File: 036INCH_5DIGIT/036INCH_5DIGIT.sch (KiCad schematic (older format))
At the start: 10 parts, among them J1 Conn_01x04_Female, J2 Conn_01x04_Male, U2 TM1637

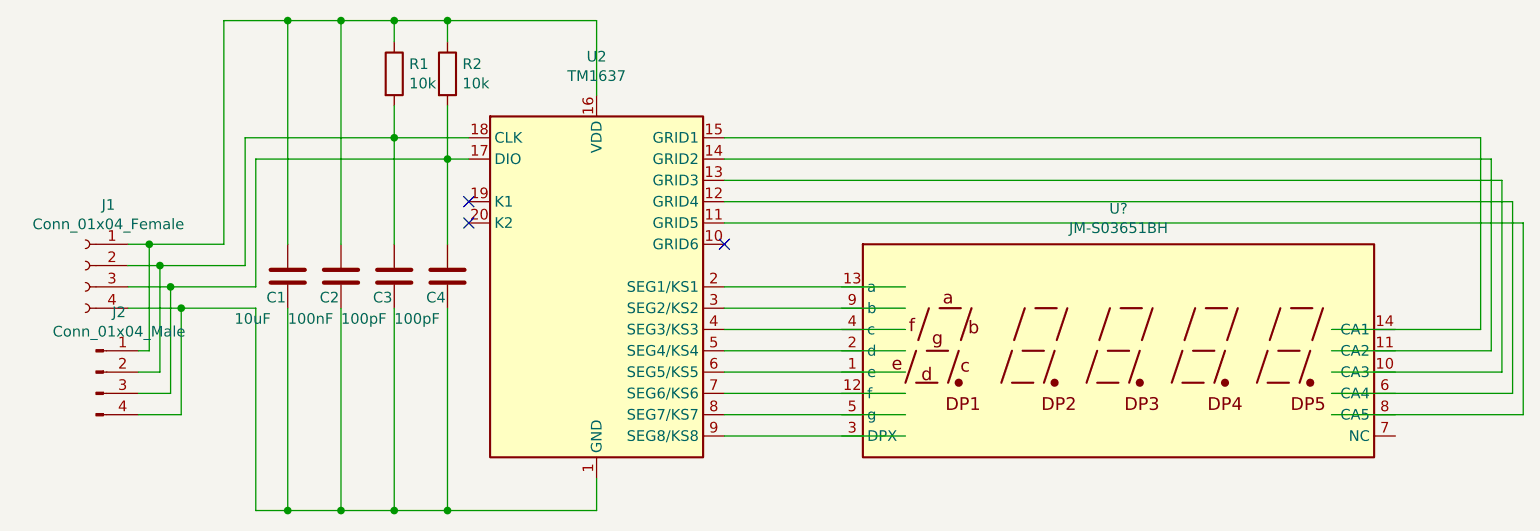
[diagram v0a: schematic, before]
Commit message: jingmei display symbol finished
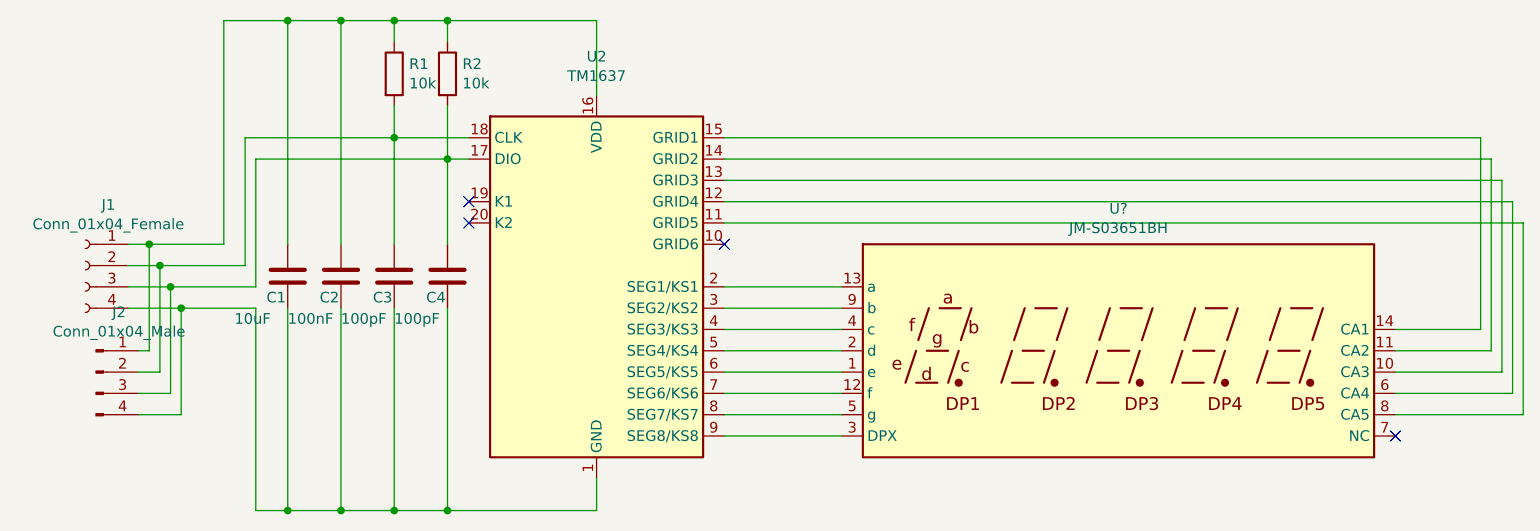
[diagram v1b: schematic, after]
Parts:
- removed U?: JM-S03651BH, JINGMEI:JM-S03651BH, symbol jingmei:JM-S03651BH
- added U?: JM-S03651BH, JINGMEI:JM-S03651BH, symbol jingmei:JM-S03651BH
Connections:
- no-connect marks 3 -> 4
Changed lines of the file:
@@
 $EndComp
-Wire Wire Line
-	3600 3800 4450 3800
-Wire Wire Line
-	3600 3900 4450 3900
-Wire Wire Line
-	3600 4000 4450 4000
-Wire Wire Line
-	3600 4100 4450 4100
-Wire Wire Line
-	3600 4200 4450 4200
-Wire Wire Line
-	3600 4300 4450 4300
-Wire Wire Line
-	3600 4400 4450 4400
 Wire Wire Line
 	3600 3000 7150 3000
@@
 	1050 3800 1400 3800
 Wire Wire Line
-	6450 3900 7150 3900
-Wire Wire Line
 	7150 3900 7150 3000
 Wire Wire Line
-	6450 4000 7200 4000
-Wire Wire Line
 	7200 4000 7200 3100
 Wire Wire Line
-	6450 4100 7250 4100
-Wire Wire Line
 	7250 4100 7250 3200
 Wire Wire Line
-	3600 3700 4450 3700
-Wire Wire Line
-	6450 4200 7300 4200
-Wire Wire Line
 	7300 4200 7300 3300
 Wire Wire Line
 	7300 3300 3600 3300
 Wire Wire Line
-	6450 4300 7350 4300
-Wire Wire Line
 	7350 3400 3600 3400
 Wire Wire Line
 	7350 4300 7350 3400
+Wire Wire Line
+	6750 3900 7150 3900
+Wire Wire Line
+	6750 4000 7200 4000
+Wire Wire Line
+	6750 4100 7250 4100
+Wire Wire Line
+	6750 4200 7300 4200
+Wire Wire Line
+	6750 4300 7350 4300
+NoConn ~ 6750 4400
+Wire Wire Line
+	3600 3700 4150 3700
+Wire Wire Line
+	3600 3800 4150 3800
+Wire Wire Line
+	3600 3900 4150 3900
+Wire Wire Line
+	3600 4000 4150 4000
+Wire Wire Line
+	3600 4100 4150 4100
+Wire Wire Line
+	3600 4200 4150 4200
+Wire Wire Line
+	3600 4300 4150 4300
+Wire Wire Line
+	3600 4400 4150 4400
 $Comp
 L jingmei:JM-S03651BH U?
-U 1 1 6190C8CE
+U 1 1 6192D4B7
 P 5450 4000
 F 0 "U?" H 5450 4667 50  0000 C CNN

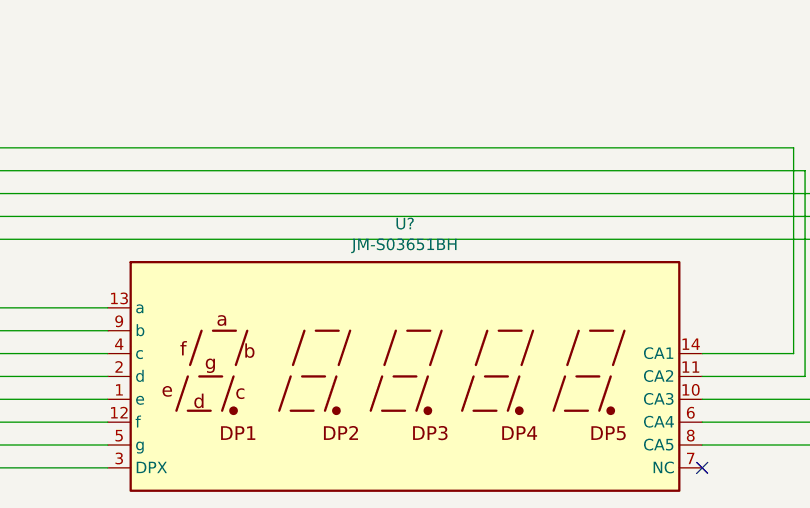
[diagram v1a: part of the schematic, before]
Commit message: starting placing elements in pcb
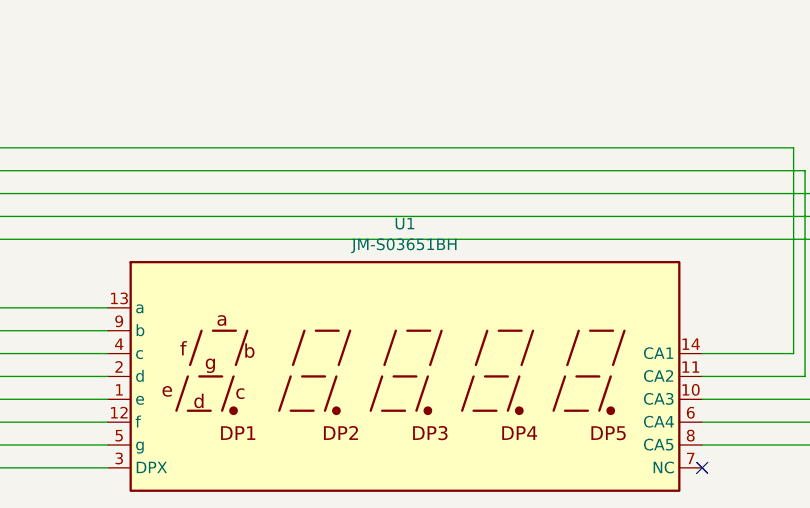
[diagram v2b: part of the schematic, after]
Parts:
- gave numbers to parts that had none: 1
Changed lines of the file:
@@
 	3600 4400 4150 4400
 $Comp
-L jingmei:JM-S03651BH U?
+L jingmei:JM-S03651BH U1
 U 1 1 6192D4B7
 P 5450 4000
-F 0 "U?" H 5450 4667 50  0000 C CNN
+F 0 "U1" H 5450 4667 50  0000 C CNN
 F 1 "JM-S03651BH" H 5450 4576 50  0000 C CNN
 F 2 "JINGMEI:JM-S03651BH" H 5450 3400 50  0001 C CNN
